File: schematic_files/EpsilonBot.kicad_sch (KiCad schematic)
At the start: 14 parts, among them J1 USB C PD Modulle, J2 Conn_01x05, J3 MOTOR_L, J4 MOTOR_R, SW1 SW_SPDT, U1 Radxa_ROCK5B, U2 Buck Converter

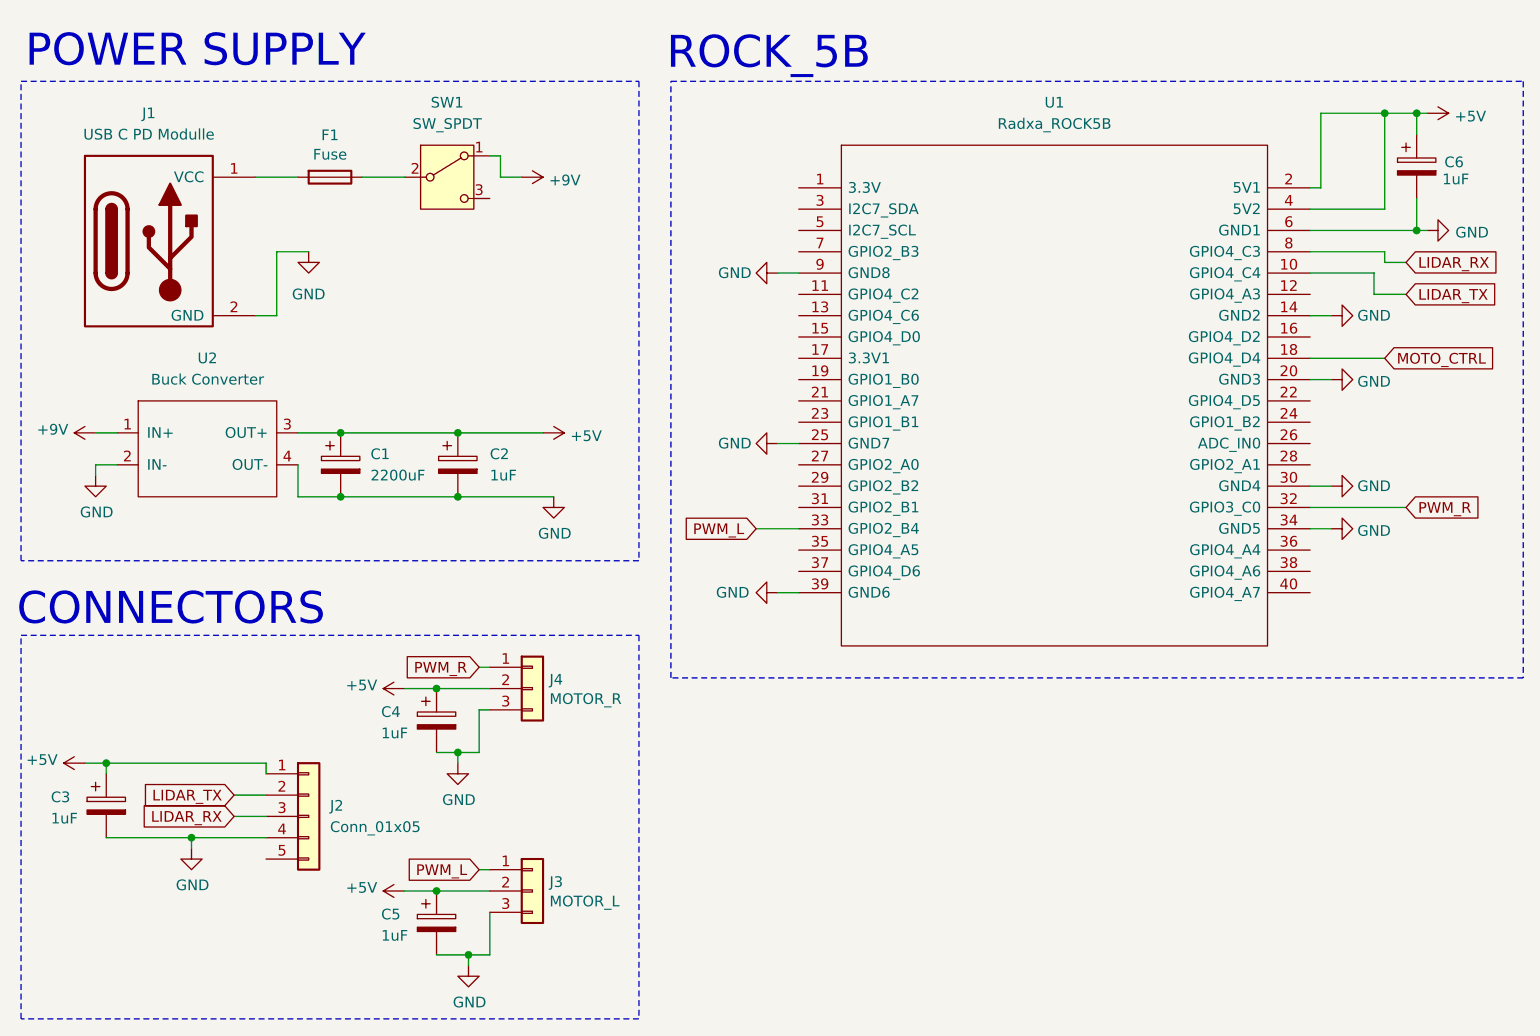
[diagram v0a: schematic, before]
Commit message: Updated PCB layout for the RPI
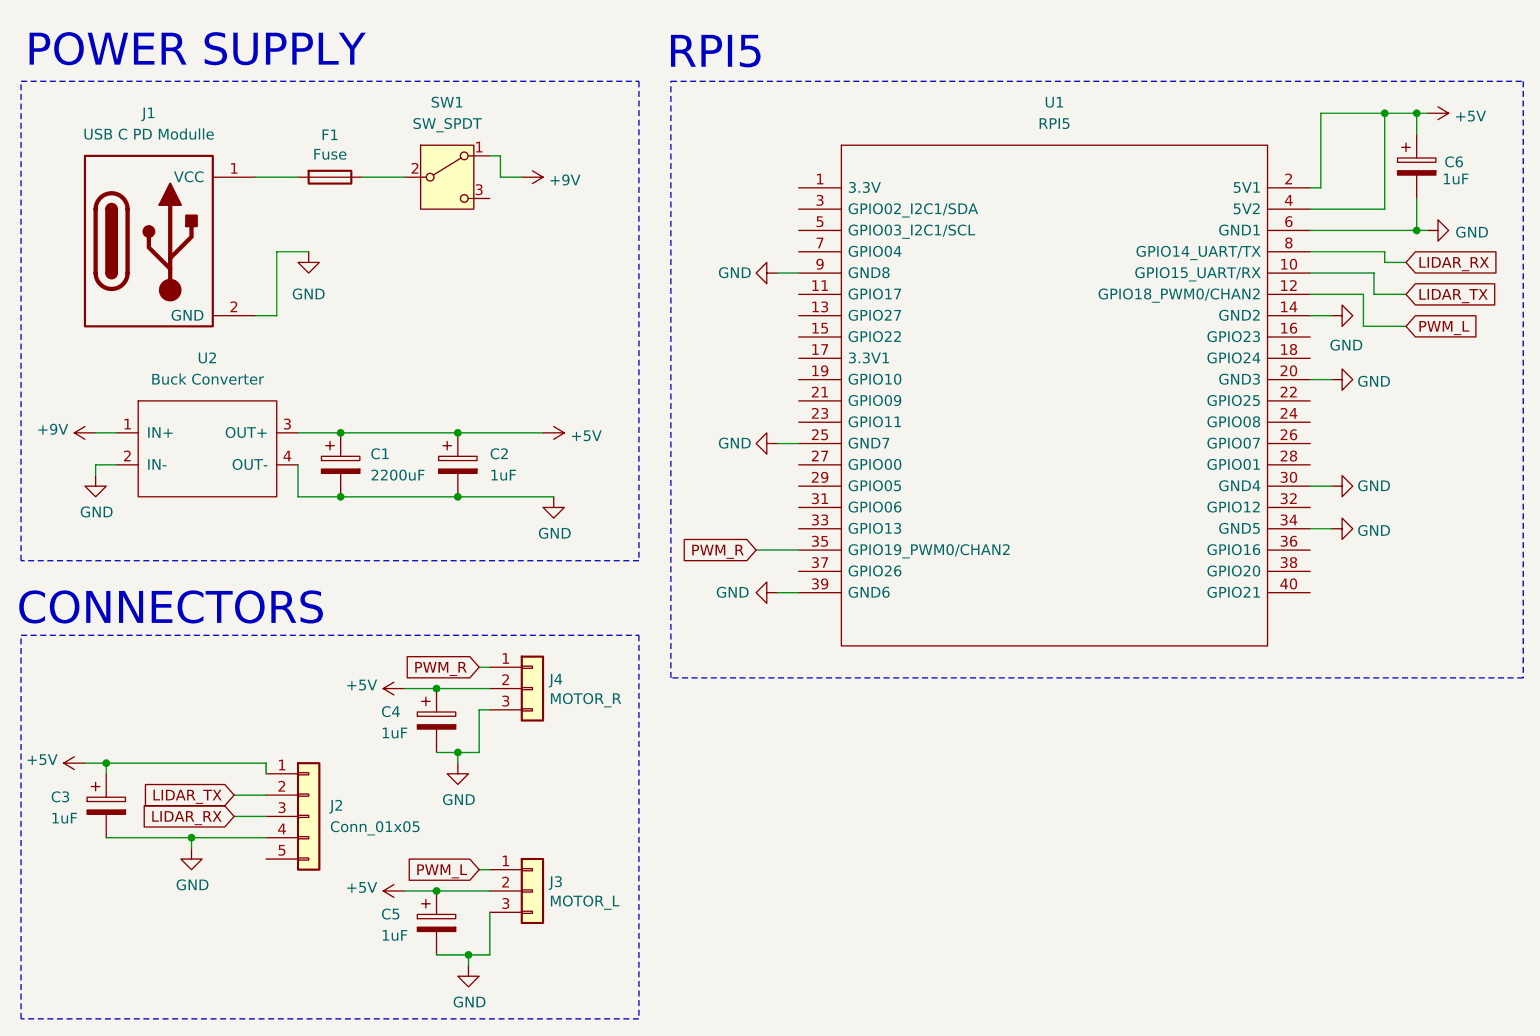
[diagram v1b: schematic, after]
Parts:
- U1: value Radxa_ROCK5B -> RPI5; footprint deltabot:ROCK_5B -> epsilon:RPI5; symbol radxa_rock5b.lib:Radxa_ROCK5B -> EpsilonBot:RPI5; Manufacturer_Part_Number ROCK5B V1.3 -> RPI5
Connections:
- net PWM_L: now also U1.12 (GPIO18_PWM0/CHAN2); no longer U1.33 (GPIO2_B4)
- net PWM_R: now also U1.35 (GPIO19_PWM0/CHAN2); no longer U1.32 (GPIO3_C0)
- net MOTO_CTRL: no longer names the net of U1.18 (GPIO24)
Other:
- note added: "RPI5"
- note removed: "ROCK_5B"

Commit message: Added missing files
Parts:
- added D1: LED, LED_THT:LED_D5.0mm_Clear, symbol Device:LED
- added R1: 330R, Resistor_THT:R_Axial_DIN0207_L6.3mm_D2.5mm_P10.16mm_Horizontal, symbol Device:R
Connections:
- net +5V: now also R1.1
- net GND: now also D1.1 (K)
- new net: D1.2 (A), R1.2
